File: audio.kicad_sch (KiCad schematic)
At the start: 100 parts, among them CN1 LEFT_JOY, CN2 RIGHT_JOY, CN3 RIGHT, CN4 LEFT, Q301 2N3906, Q321 MPF102, Q331 MPF102, Q921 MMBFJ113, Q931 MMBFJ113, U14 LF347, U15 74LS157, U3 PAULA, U38 MC1488

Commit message: more work on BOM done
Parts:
- D400, D401, D402, D403: MFG Name (none) -> DIODES INC; MFG Part Num (none) -> SM05-7; Mouser (none) -> 621-SM05-7
- R301, R302: MFG Name (none) -> YAGEO; MFG Part Num (none) -> MFR-25FBF52-10R; Mouser (none) -> 603-MFR-25FBF52-10R
- R303, R304, R305, R324, R334: MFG Name (none) -> YAGEO; MFG Part Num (none) -> MFR-25FBF52-1K; Mouser (none) -> 603-MFR-25FBF52-1K
- R306, R308, R322, R323, R332, R333, R339: MFG Name (none) -> YAGEO; MFG Part Num (none) -> MFR-25FBF52-10K; Mouser (none) -> 603-MFR-25FBF52-10K
- R307: MFG Name (none) -> YAGEO; MFG Part Num (none) -> MFR-25FBF52-2K7; Mouser (none) -> 603-MFR-25FBF52-2K7
- R309: MFG Name (none) -> VISHAY; MFG Part Num (none) -> PR02000201009JA100; Mouser (none) -> 594-5083NW10R00JA100
- R321, R331: MFG Name (none) -> YAGEO; MFG Part Num (none) -> MFR-25FRF52-360R; Mouser (none) -> 603-MFR-25FRF52-360R
- R325, R335: MFG Name (none) -> YAGEO; MFG Part Num (none) -> MFR-25FBF52-390R; Mouser (none) -> 603-MFR-25FBF52-390R
- R326, R336: MFG Name (none) -> YAGEO; MFG Part Num (none) -> MFR-25FBF52-470K; Mouser (none) -> 603-MFR-25FBF52-470K
- R401, R408: MFG Name (none) -> VISHAY; MFG Part Num (none) -> PR02000204708JA100; Mouser (none) -> 594-5083NW4R700JA100

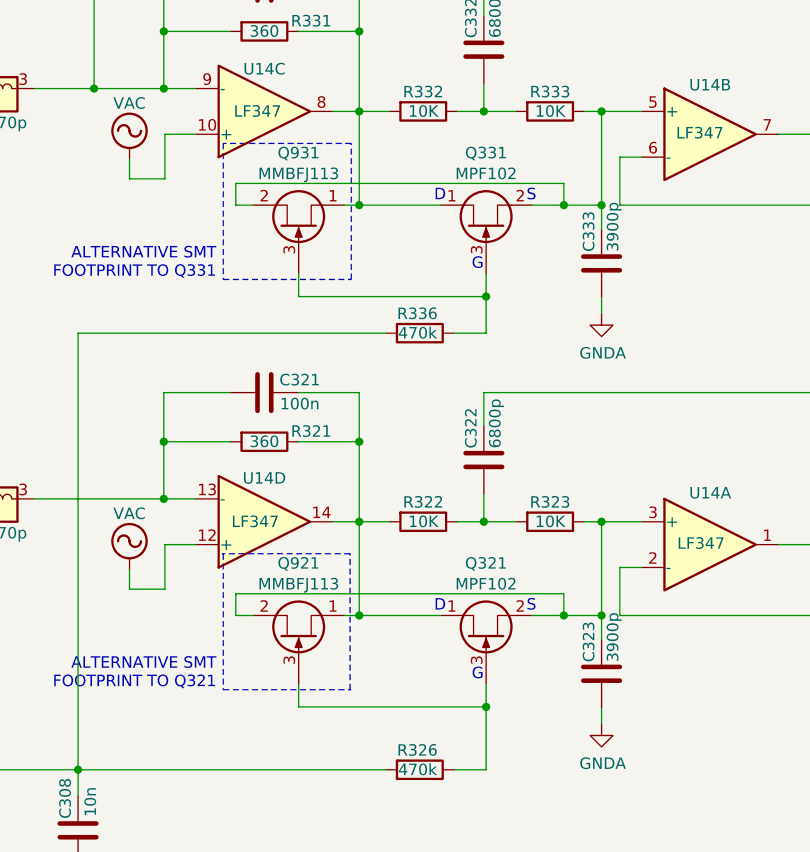
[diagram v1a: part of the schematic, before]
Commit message: More BOM work
I am marking optional components as DNP to get some overview
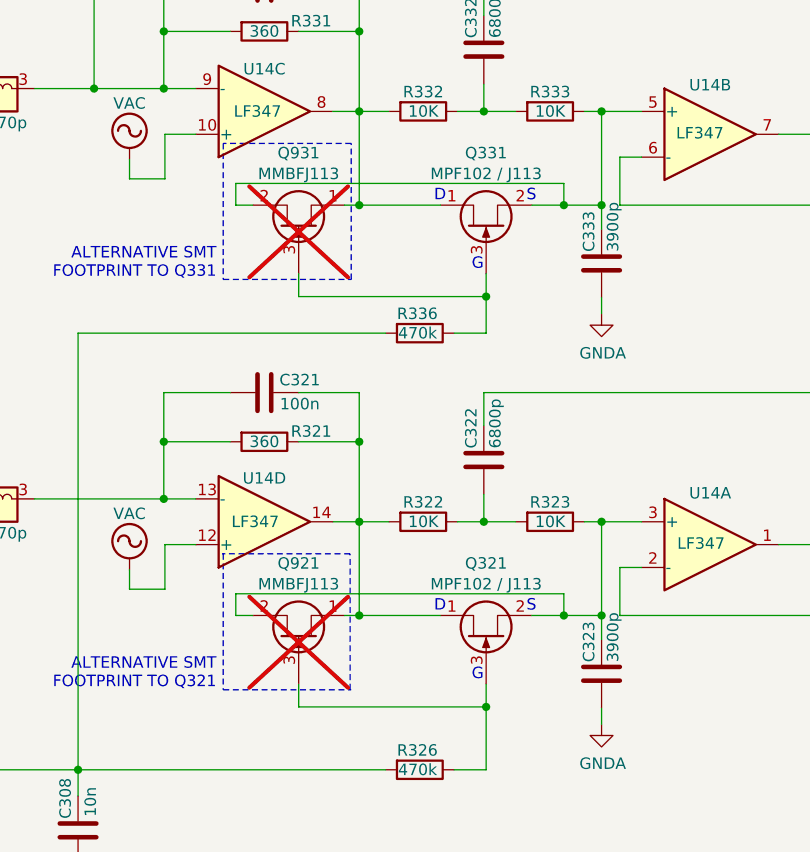
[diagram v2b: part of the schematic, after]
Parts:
- E302, E303, E411, E412, E413, E414, E421, E422, E423, E424: Mouser (none) -> 81-DSS1NB32A682Q91A
- E305, E306: Mouser (none) -> 81-DSS1NB32A271Q91A
- E401, E408: Mouser (none) -> 81-DSS1NB32A103Q91A
- E415, E416, E417, E425, E426, E427, E441, E442, E443, E444: Mouser (none) -> 81-DSS1NB32A471Q91A
- FB802: MFG Name (none) -> FAIR-RITE; MFG Part Num (none) -> 2743007111; Mouser (none) -> 623-2743007111
- Q301: MFG Name (none) -> ONSEMI; MFG Part Num (none) -> 2N3906BU; Mouser (none) -> 512-2N3906BU
- Q321, Q331: value MPF102 -> MPF102 / J113; MFG Name (none) -> ONSEMI; MFG Part Num (none) -> J113; Mouser (none) -> 512-J113
- Q921, Q931: now not fitted
- U3: MFG Name (none) -> COMMODORE
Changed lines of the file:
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@@
 			)
 		)
+		(property "MFG Name" "COMMODORE"
+			(at 79.375 143.637 0)
+			(effects
+				(font
+					(size 1.27 1.27)
+				)
+				(hide yes)
+			)
+		)
 		(pin "26"
 		)
@@
 			)
 		)
-		(property "Mouser" ""
+		(property "Mouser" "623-2743007111 "
+			(at 109.982 204.978 0)
+			(effects
+				(font
+					(size 1.27 1.27)
+				)
+				(hide yes)
+			)
+		)
+		(property "MFG Name" "FAIR-RITE"
+			(at 109.982 204.978 0)
+			(effects
+				(font
+					(size 1.27 1.27)
+				)
+				(hide yes)
+			)
+		)
+		(property "MFG Part Num" "2743007111 "
 			(at 109.982 204.978 0)
 			(effects
@@
 			)
 		)
-		(property "Mouser" ""
+		(property "Mouser" "81-DSS1NB32A471Q91A "
 			(at 180.086 50.8 0)
 			(effects
@@
 			)
 		)
-		(property "Mouser" ""
+		(property "Mouser" "81-DSS1NB32A103Q91A "
 			(at 189.357 58.42 0)
 			(effects
@@
 			)
 		)
-		(property "Mouser" ""
+		(property "Mouser" "81-DSS1NB32A471Q91A "
 			(at 180.086 68.58 0)
 			(effects
@@
 			)
 		)
-		(property "Mouser" ""
+		(property "Mouser" "81-DSS1NB32A471Q91A "
 			(at 192.532 74.93 0)
 			(effects
@@
 			)
 		)
-		(property "Mouser" ""
+		(property "Mouser" "81-DSS1NB32A471Q91A "
 			(at 180.086 107.823 0)
 			(effects
@@
 			)
 		)
-		(property "Mouser" ""
+		(property "Mouser" "81-DSS1NB32A103Q91A "
 			(at 189.357 115.062 0)
 			(effects
@@
 			)
 		)
-		(property "Mouser" ""
+		(property "Mouser" "81-DSS1NB32A471Q91A "
 			(at 180.086 125.222 0)
 			(effects
@@
 			)
 		)
-		(property "Mouser" ""
+		(property "Mouser" "81-DSS1NB32A471Q91A "
 			(at 192.532 131.826 0)
 			(effects
@@
 			)
 		)
-		(property "Mouser" ""
+		(property "Mouser" "81-DSS1NB32A682Q91A "
 			(at 244.983 42.799 0)
 			(effects
@@
 			)
 		)
-		(property "Mouser" ""
+		(property "Mouser" "81-DSS1NB32A682Q91A "
 			(at 244.983 53.721 0)
 			(effects
@@
 			)
 		)
-		(property "Mouser" ""
+		(property "Mouser" "81-DSS1NB32A682Q91A "
 			(at 244.983 63.881 0)
 			(effects
@@
 			)
 		)
-		(property "Mouser" ""
+		(property "Mouser" "81-DSS1NB32A682Q91A "
 			(at 244.983 74.549 0)
 			(effects
@@
 			)
 		)
-		(property "Mouser" ""
+		(property "Mouser" "81-DSS1NB32A682Q91A "
 			(at 244.983 99.441 0)
 			(effects
@@
 			)
 		)
-		(property "Mouser" ""
+		(property "Mouser" "81-DSS1NB32A682Q91A "
 			(at 244.983 110.363 0)
 			(effects
@@
 			)
 		)
-		(property "Mouser" ""
+		(property "Mouser" "81-DSS1NB32A682Q91A "
 			(at 244.983 120.523 0)
 			(effects
@@
 			)
 		)
-		(property "Mouser" ""
+		(property "Mouser" "81-DSS1NB32A682Q91A "
 			(at 244.983 131.191 0)
 			(effects
@@
 			)
 		)
+		(property "MFG Name" "COMMODORE"
+			(at 28.575 54.864 0)
+			(effects
+				(font
+					(size 1.27 1.27)
+				)
+				(hide yes)
+			)
+		)
 		(pin "42"
 		)
@@
 			)
 		)
-		(property "Mouser" ""
+		(property "Mouser" "81-DSS1NB32A471Q91A "
 			(at 340.868 68.072 0)
 			(effects
@@
 			)
 		)
-		(property "Mouser" ""
+		(property "Mouser" "81-DSS1NB32A471Q91A "
 			(at 340.868 78.994 0)
 			(effects
@@
 			)
 		)
-		(property "Mouser" ""
+		(property "Mouser" "81-DSS1NB32A471Q91A "
 			(at 340.868 89.154 0)
 			(effects
@@
 			)
 		)
-		(property "Mouser" ""
+		(property "Mouser" "81-DSS1NB32A471Q91A "
 			(at 340.868 99.822 0)
 			(effects
@@
 			)
 		)
-		(property "Mouser" ""
+		(property "Mouser" "81-DSS1NB32A271Q91A"
 			(at 160.274 178.308 0)
 			(effects
@@
 			)
 		)
-		(property "Mouser" ""
+		(property "Mouser" "81-DSS1NB32A271Q91A"
 			(at 160.274 223.901 0)
 			(effects
@@
 			)
 		)
-		(property "Mouser" ""
+		(property "Mouser" "81-DSS1NB32A682Q91A "
 			(at 305.308 228.981 0)
 			(effects
@@
 			)
 		)
-		(property "Value" "MPF102"
+		(property "Value" "MPF102 / J113"
 			(at 218.059 230.8352 90)
 			(effects
@@
 			)
 		)
-		(property "Mouser" ""
+		(property "Mouser" "512-J113 "
+			(at 218.059 236.855 90)
+			(effects
+				(font
+					(size 1.27 1.27)
+				)
+				(hide yes)
+			)
+		)
+		(property "MFG Name" "ONSEMI"
+			(at 218.059 236.855 90)
+			(effects
+				(font
+					(size 1.27 1.27)
+				)
+				(hide yes)
+			)
+		)
+		(property "MFG Part Num" "J113"
 			(at 218.059 236.855 90)
 			(effects
@@
 			)
 		)
-		(property "Mouser" ""
+		(property "Mouser" "81-DSS1NB32A682Q91A "
 			(at 305.308 183.388 0)
 			(effects
@@
 			)
 		)
-		(property "Value" "MPF102"
+		(property "Value" "MPF102 / J113"
 			(at 218.059 185.2422 90)
 			(effects
@@
 			)
 		)
-		(property "Mouser" ""
+		(property "Mouser" "512-J113 "
+			(at 218.059 191.262 90)
+			(effects
+				(font
+					(size 1.27 1.27)
+				)
+				(hide yes)
+			)
+		)
+		(property "MFG Name" "ONSEMI"
+			(at 218.059 191.262 90)
+			(effects
+				(font
+					(size 1.27 1.27)
+				)
+				(hide yes)
+			)
+		)
+		(property "MFG Part Num" "J113"
 			(at 218.059 191.262 90)
 			(effects
@@
 			)
 		)
-		(property "Mouser" ""
+		(property "Mouser" "512-2N3906BU "
+			(at 127.889 235.839 0)
+			(effects
+				(font
+					(size 1.27 1.27)
+				)
+				(hide yes)
+			)
+		)
+		(property "MFG Name" "ONSEMI"
+			(at 127.889 235.839 0)
+			(effects
+				(font
+					(size 1.27 1.27)
+				)
+				(hide yes)
+			)
+		)
+		(property "MFG Part Num" "2N3906BU "
 			(at 127.889 235.839 0)
 			(effects
@@
 		(in_bom yes)
 		(on_board yes)
-		(dnp no)
+		(dnp yes)
 		(property "Reference" "Q931"
 			(at 197.231 182.9308 90)
@@
 		(in_bom yes)
 		(on_board yes)
-		(dnp no)
+		(dnp yes)
 		(property "Reference" "Q921"
 			(at 197.231 228.5238 90)

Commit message: BOM updates
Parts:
- RP401: MFG Name (none) -> BOURNS; MFG Part Num (none) -> 4610X-101-472LF; Mouser (none) -> 652-4610X-1LF-4.7K
- U14: MFG Part Num LF347N ??? -> LF347N; Mouser (none) -> 595-LF347N
- U15: MFG Part Num SN74HCT157NE4 -> SN74LS157N; Mouser (none) -> 595-SN74LS157N
- U3: MFG Name COMMODORE -> 3M; MFG Part Num (none) -> 4848-6000-CP; Mouser (none) -> 517-4848-6000-CP
- U38: MFG Part Num MC1488N -> SN75C188N; Mouser (none) -> 595-SN75C188N
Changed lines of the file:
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@@
 			)
 		)
-		(property "Mouser" ""
+		(property "Mouser" "517-4848-6000-CP "
 			(at 79.375 143.637 0)
 			(effects
@@
 			)
 		)
-		(property "MFG Name" "COMMODORE"
+		(property "MFG Name" "3M"
+			(at 79.375 143.637 0)
+			(effects
+				(font
+					(size 1.27 1.27)
+				)
+				(hide yes)
+			)
+		)
+		(property "MFG Part Num" "4848-6000-CP "
 			(at 79.375 143.637 0)
 			(effects
@@
 			)
 		)
-		(property "MFG Part Num" "SN74HCT157NE4"
+		(property "MFG Part Num" "SN74LS157N "
 			(at 316.357 85.725 0)
 			(effects
@@
 			)
 		)
-		(property "Mouser" ""
+		(property "Mouser" "595-SN74LS157N "
 			(at 316.357 85.725 0)
 			(effects
@@
 			)
 		)
-		(property "Mouser" ""
+		(property "Mouser" "517-4848-6000-CP "
 			(at 28.575 54.864 0)
 			(effects
@@
 			)
 		)
-		(property "MFG Name" "COMMODORE"
+		(property "MFG Name" "3M"
+			(at 28.575 54.864 0)
+			(effects
+				(font
+					(size 1.27 1.27)
+				)
+				(hide yes)
+			)
+		)
+		(property "MFG Part Num" "4848-6000-CP "
 			(at 28.575 54.864 0)
 			(effects
@@
 			)
 		)
-		(property "MFG Part Num" "LF347N ???"
+		(property "MFG Part Num" "LF347N "
 			(at 32.766 246.507 0)
 			(effects
@@
 			)
 		)
-		(property "Mouser" ""
+		(property "Mouser" "595-LF347N "
 			(at 32.766 246.507 0)
 			(effects
@@
 			)
 		)
-		(property "Mouser" ""
+		(property "Mouser" "652-4610X-1LF-4.7K"
+			(at 287.528 57.531 0)
+			(effects
+				(font
+					(size 1.27 1.27)
+				)
+				(hide yes)
+			)
+		)
+		(property "MFG Name" "BOURNS"
+			(at 287.528 57.531 0)
+			(effects
+				(font
+					(size 1.27 1.27)
+				)
+				(hide yes)
+			)
+		)
+		(property "MFG Part Num" "4610X-101-472LF "
 			(at 287.528 57.531 0)
 			(effects
@@
 			)
 		)
-		(property "MFG Part Num" "LF347N ???"
+		(property "MFG Part Num" "LF347N "
 			(at 242.951 226.441 0)
 			(effects
@@
 			)
 		)
-		(property "Mouser" ""
+		(property "Mouser" "595-LF347N "
 			(at 242.951 226.441 0)
 			(effects
@@
 			)
 		)
-		(property "MFG Part Num" "LF347N ???"
+		(property "MFG Part Num" "LF347N "
 			(at 242.951 180.848 0)
 			(effects
@@
 			)
 		)
-		(property "Mouser" ""
+		(property "Mouser" "595-LF347N "
 			(at 242.951 180.848 0)
 			(effects
@@
 			)
 		)
-		(property "MFG Part Num" "LF347N ???"
+		(property "MFG Part Num" "LF347N "
 			(at 193.421 178.308 0)
 			(effects
@@
 			)
 		)
-		(property "Mouser" ""
+		(property "Mouser" "595-LF347N "
 			(at 193.421 178.308 0)
 			(effects
@@
 			)
 		)
-		(property "MFG Part Num" "LF347N ???"
+		(property "MFG Part Num" "LF347N "
 			(at 193.421 223.901 0)
 			(effects
@@
 			)
 		)
-		(property "Mouser" ""
+		(property "Mouser" "595-LF347N "
 			(at 193.421 223.901 0)
 			(effects
@@
 			)
 		)
-		(property "MFG Part Num" "MC1488N"
+		(property "MFG Part Num" "SN75C188N "
 			(at 97.409 235.839 0)
 			(effects
@@
 			)
 		)
-		(property "Mouser" ""
+		(property "Mouser" "595-SN75C188N "
 			(at 97.409 235.839 0)
 			(effects
@@
 			)
 		)
-		(property "MFG Part Num" "SN74HCT157NE4"
+		(property "MFG Part Num" "SN74LS157N "
 			(at 378.46 84.963 0)
 			(effects
@@
 			)
 		)
-		(property "Mouser" ""
+		(property "Mouser" "595-SN74LS157N "
 			(at 378.46 84.963 0)
 			(effects

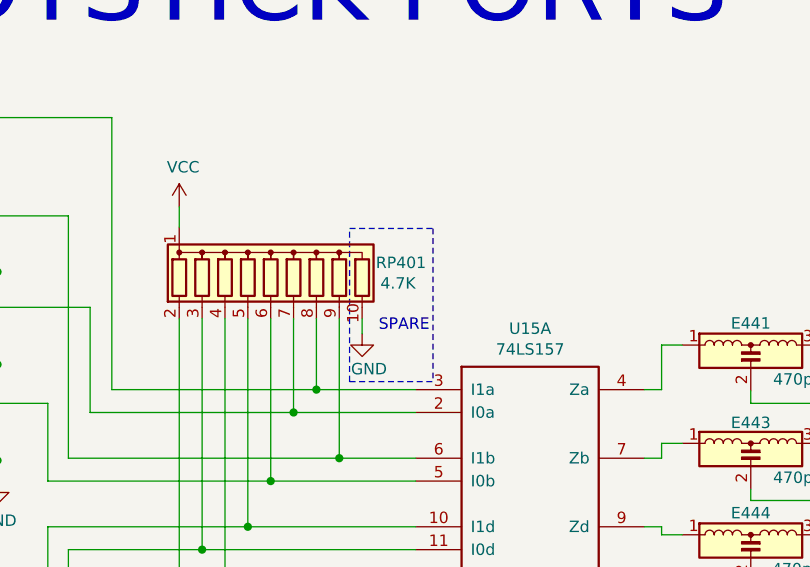
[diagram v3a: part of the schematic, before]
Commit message: replaced commodore hybrid with OpenAmigaVideoHybrid
decided to place address pullups for better EPROM capability
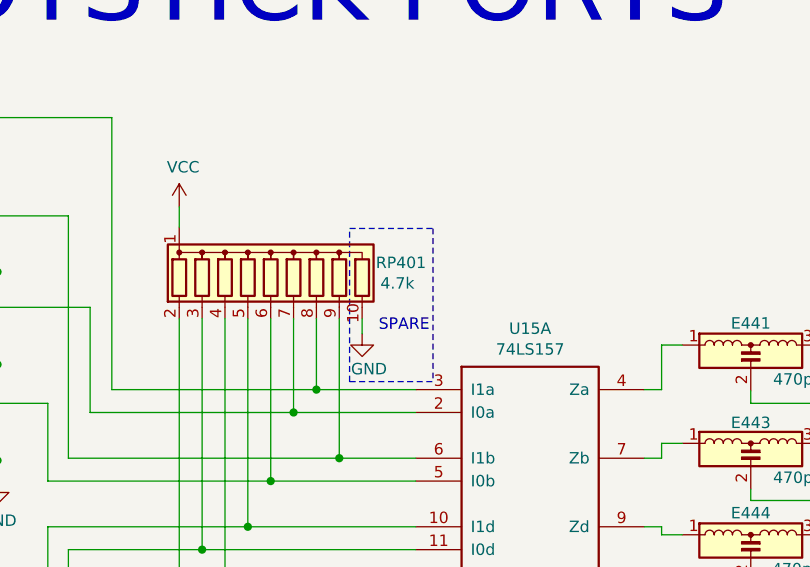
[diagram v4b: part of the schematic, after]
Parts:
- RP401: value 4.7K -> 4.7k
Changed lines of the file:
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@@
 			)
 		)
-		(property "Value" "4.7K"
+		(property "Value" "4.7k"
 			(at 299.72 58.674 0)
 			(effects

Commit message: more silkscreen work
removed sockets for standard IC's
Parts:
- U14, U38: footprint Package_DIP:DIP-14_W7.62mm_Socket_LongPads -> Package_DIP:DIP-14_W7.62mm_LongPads
- U15: footprint Package_DIP:DIP-16_W7.62mm_Socket_LongPads -> Package_DIP:DIP-16_W7.62mm_LongPads
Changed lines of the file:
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@@
 	(title_block
 		(title "Rämixx500_max")
-		(date "2026-04-09")
+		(date "2026-04-26")
 		(rev "3")
 		(company "SukkoPera")
@@
 			)
 		)
-		(property "Footprint" "Package_DIP:DIP-16_W7.62mm_Socket_LongPads"
+		(property "Footprint" "Package_DIP:DIP-16_W7.62mm_LongPads"
 			(at 316.357 85.725 0)
 			(effects
@@
 			)
 		)
-		(property "Footprint" "Package_DIP:DIP-14_W7.62mm_Socket_LongPads"
+		(property "Footprint" "Package_DIP:DIP-14_W7.62mm_LongPads"
 			(at 31.496 243.967 0)
 			(effects
@@
 			)
 		)
-		(property "Footprint" "Package_DIP:DIP-14_W7.62mm_Socket_LongPads"
+		(property "Footprint" "Package_DIP:DIP-14_W7.62mm_LongPads"
 			(at 241.681 223.901 0)
 			(effects
@@
 			)
 		)
-		(property "Footprint" "Package_DIP:DIP-14_W7.62mm_Socket_LongPads"
+		(property "Footprint" "Package_DIP:DIP-14_W7.62mm_LongPads"
 			(at 241.681 178.308 0)
 			(effects
@@
 			)
 		)
-		(property "Footprint" "Package_DIP:DIP-14_W7.62mm_Socket_LongPads"
+		(property "Footprint" "Package_DIP:DIP-14_W7.62mm_LongPads"
 			(at 192.151 180.848 0)
 			(effects
@@
 			)
 		)
-		(property "Footprint" "Package_DIP:DIP-14_W7.62mm_Socket_LongPads"
+		(property "Footprint" "Package_DIP:DIP-14_W7.62mm_LongPads"
 			(at 192.151 226.441 0)
 			(effects
@@
 			)
 		)
-		(property "Footprint" "Package_DIP:DIP-14_W7.62mm_Socket_LongPads"
+		(property "Footprint" "Package_DIP:DIP-14_W7.62mm_LongPads"
 			(at 97.409 235.839 0)
 			(effects
@@
 			)
 		)
-		(property "Footprint" "Package_DIP:DIP-16_W7.62mm_Socket_LongPads"
+		(property "Footprint" "Package_DIP:DIP-16_W7.62mm_LongPads"
 			(at 378.46 84.963 0)
 			(effects

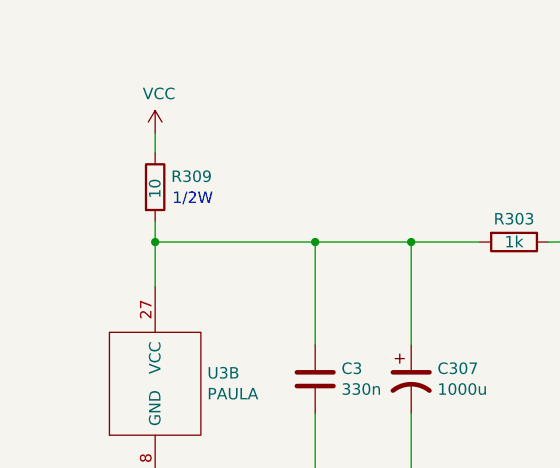
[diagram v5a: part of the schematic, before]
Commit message: fixed R309 wrong value
Replaced too big 2W resistors with better fitting 1W resistors
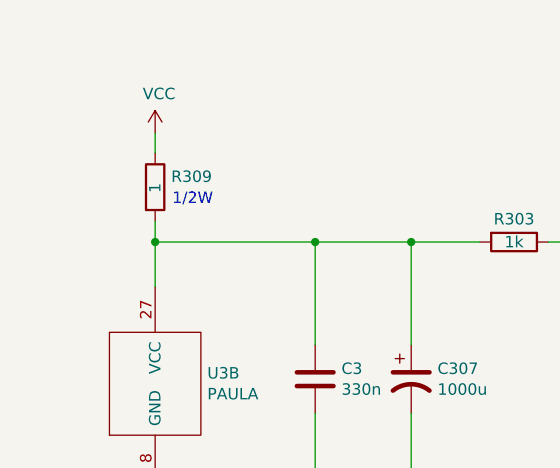
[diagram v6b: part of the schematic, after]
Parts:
- R309: value 10 -> 1; MFG Part Num PR02000201009JA100 -> PR01000101008JA500; Mouser 594-5083NW10R00JA100 -> 594-PR01000101008JA5
- R401, R408: MFG Part Num PR02000204708JA100 -> PR01000104708JA500; Mouser 594-5083NW4R700JA100 -> 594-PR01000104708JA5
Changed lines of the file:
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@@
 			)
 		)
-		(property "Mouser" "594-5083NW4R700JA100"
+		(property "Mouser" "594-PR01000104708JA5"
 			(at 168.275 42.164 90)
 			(effects
@@
 			)
 		)
-		(property "MFG Part Num" "PR02000204708JA100 "
+		(property "MFG Part Num" "PR01000104708JA500 "
 			(at 168.275 42.164 90)
 			(effects
@@
 			)
 		)
-		(property "Mouser" "594-5083NW4R700JA100"
+		(property "Mouser" "594-PR01000104708JA5"
 			(at 168.275 98.806 90)
 			(effects
@@
 			)
 		)
-		(property "MFG Part Num" "PR02000204708JA100 "
+		(property "MFG Part Num" "PR01000104708JA500 "
 			(at 168.275 98.806 90)
 			(effects
@@
 			)
 		)
-		(property "Value" "10"
-			(at 28.575 33.655 90)
+		(property "Value" "1"
+			(at 28.575 33.02 90)
 			(effects
 				(font
@@
 			)
 		)
-		(property "Mouser" "594-5083NW10R00JA100 "
+		(property "Mouser" "594-PR01000101008JA5"
 			(at 28.575 32.385 0)
 			(effects
@@
 			)
 		)
-		(property "MFG Part Num" "PR02000201009JA100"
+		(property "MFG Part Num" "PR01000101008JA500"
 			(at 28.575 32.385 0)
 			(effects
